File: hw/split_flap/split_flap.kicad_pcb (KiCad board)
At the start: 2 copper layers, 104.5 x 98.3 mm, 42 parts, among them J1 Conn_01x02, J10 Conn_01x05, J11 Conn_01x05, J12 Conn_01x05, J13 Conn_01x05, J14 Conn_01x05, J15 Conn_01x05, J16 Conn_01x05, J19 POWER, J2 Conn_01x02, J3 Conn_01x02, J4 Conn_01x02, J5 Conn_01x02, J6 Conn_01x02, J7 Conn_01x02, J8 Conn_01x02, J9 Conn_01x05, SW1 SW_RESET, U1 PCF8574, U10 ULN2803A, U2 NodeMCU_1.0_(ESP-12E), U3 PCF8574, U4 ULN2803A, U5 PCF8574, U6 ULN2803A, U7 PCF8574, U8 ULN2803A, U9 PCF8574

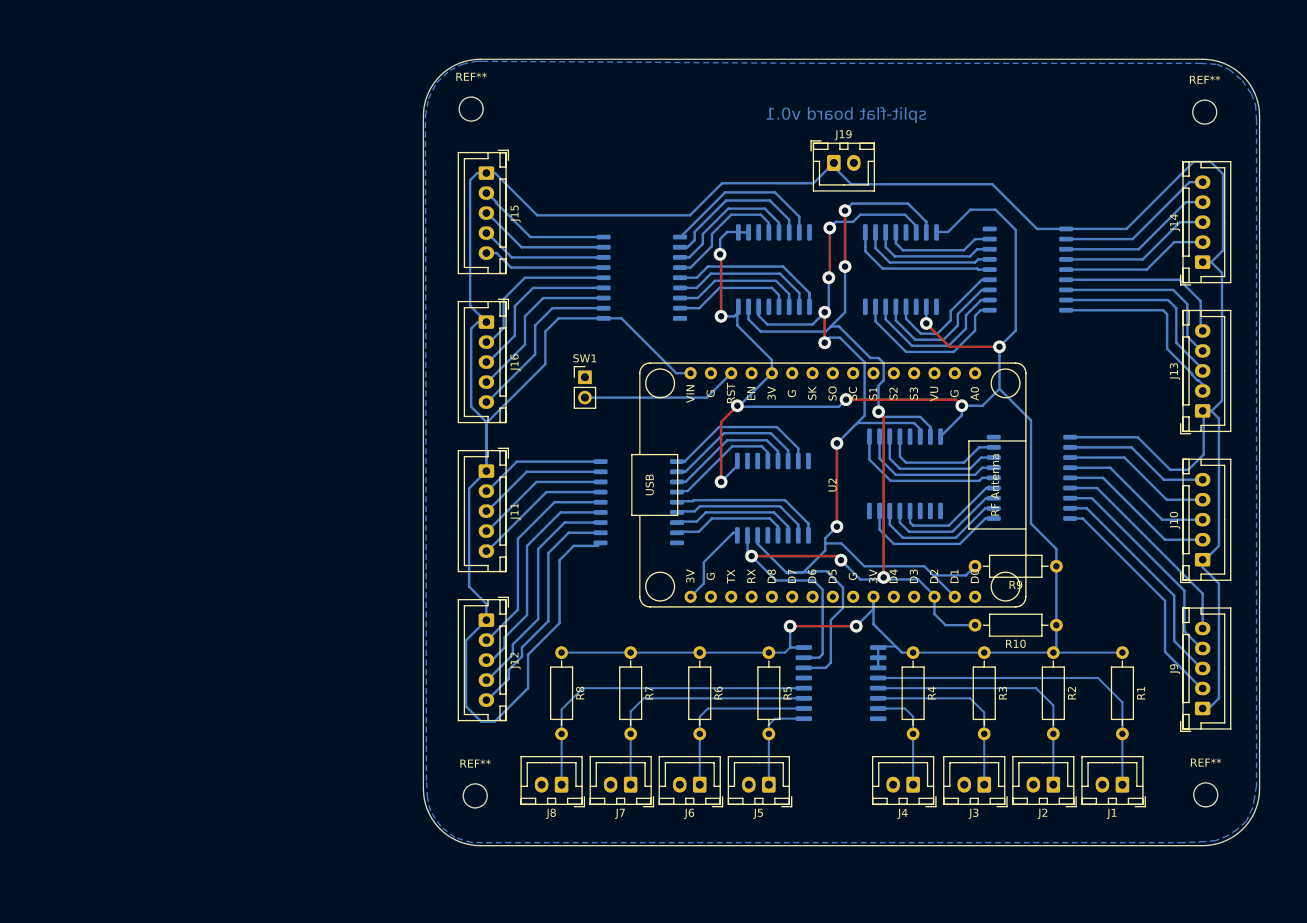
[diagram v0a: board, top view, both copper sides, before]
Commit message: Add missing Interrupt line
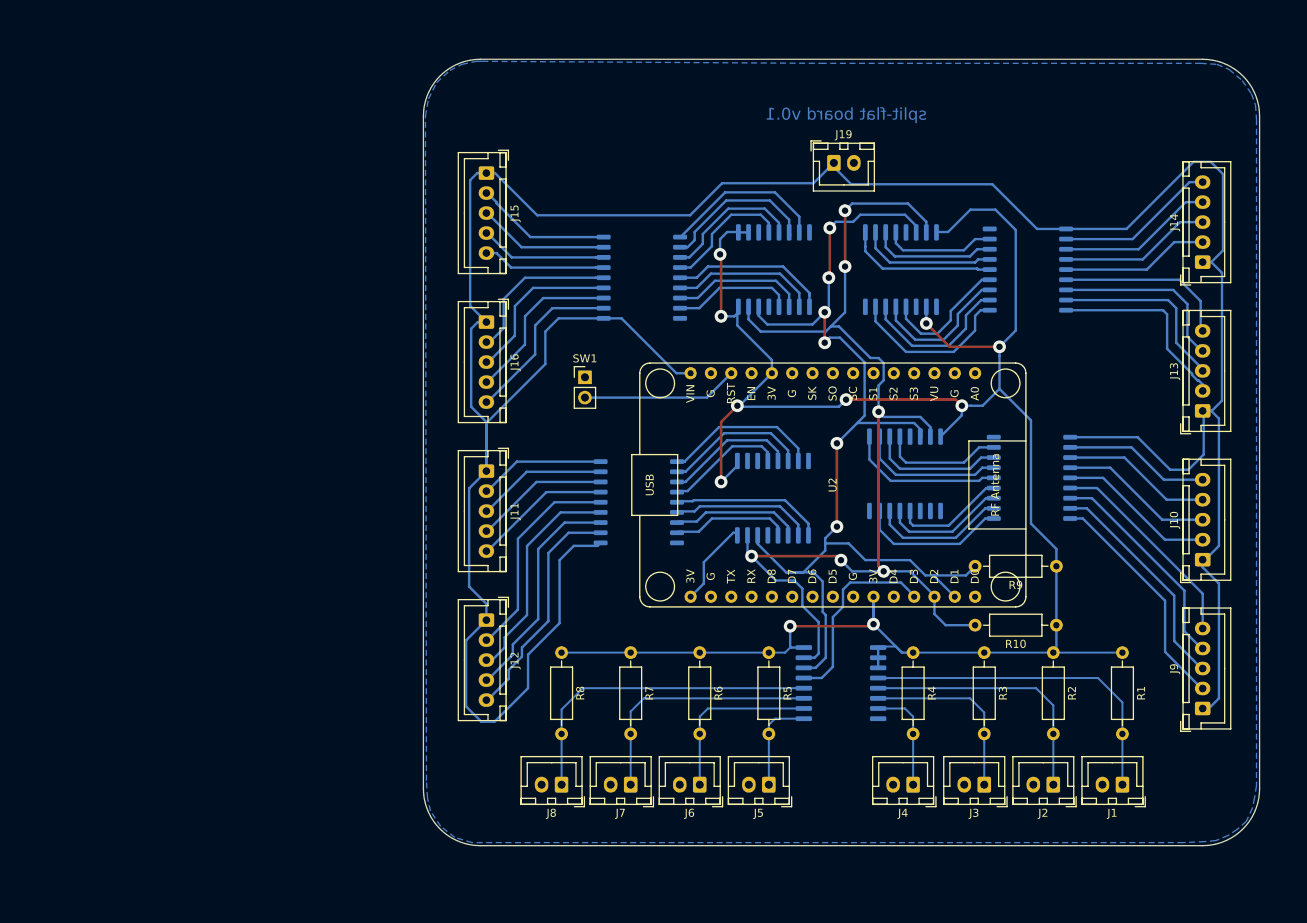
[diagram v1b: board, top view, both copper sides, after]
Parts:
- removed REF** (x4): MountingHole_3mm, MountingHole:MountingHole_3mm
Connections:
- U1 pad 13: (no net) -> /INT
- U2 pad 27: (no net) -> /INT
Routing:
- net /INT: track 0.00 -> 24.5 mm
- net /SCL: track 137.1 -> 133.4 mm
- net /SDA: track 142.3 -> 138.9 mm
- net +3V3: track 264.5 -> 265.6 mm

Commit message: hw: Supercharge PCB !
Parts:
- removed SW1: SW_RESET, Connector_PinHeader_2.54mm:PinHeader_1x02_P2.54mm_Vertical
- added J17: Conn_01x05, Connector_JST:JST_XH_B5B-XH-A_1x05_P2.50mm_Vertical, F.Cu at (144.4, 99.7)
- added J18: Conn_01x05, Connector_JST:JST_XH_B5B-XH-A_1x05_P2.50mm_Vertical, F.Cu at (194.9, 63.8)
- added J20: Conn_01x05, Connector_JST:JST_XH_B5B-XH-A_1x05_P2.50mm_Vertical, F.Cu at (179.5, 45.8)
- added J21: Conn_01x05, Connector_JST:JST_XH_B5B-XH-A_1x05_P2.50mm_Vertical, F.Cu at (108.3, 45.6)
- added J22: Conn_01x05, Connector_JST:JST_XH_B5B-XH-A_1x05_P2.50mm_Vertical, F.Cu at (102.1, 53.6)
- added J23: Conn_01x02, Connector_JST:JST_XH_B2B-XH-A_1x02_P2.50mm_Vertical, F.Cu at (130.6, 91.6)
- added J24: Conn_01x02, Connector_JST:JST_XH_B2B-XH-A_1x02_P2.50mm_Vertical, F.Cu at (130.6, 83.1)
- added J25: Conn_01x02, Connector_JST:JST_XH_B2B-XH-A_1x02_P2.50mm_Vertical, F.Cu at (166.5, 80.4)
- added J26: Conn_01x02, Connector_JST:JST_XH_B2B-XH-A_1x02_P2.50mm_Vertical, F.Cu at (166.5, 88.9)
- added R11: R, Resistor_THT:R_Axial_DIN0207_L6.3mm_D2.5mm_P10.16mm_Horizontal, F.Cu at (126.0, 97.3)
- added R12: R, Resistor_THT:R_Axial_DIN0207_L6.3mm_D2.5mm_P10.16mm_Horizontal, F.Cu at (126.0, 74.8)
- added R13: R, Resistor_THT:R_Axial_DIN0207_L6.3mm_D2.5mm_P10.16mm_Horizontal, F.Cu at (171.2, 74.5)
- added R14: R, Resistor_THT:R_Axial_DIN0207_L6.3mm_D2.5mm_P10.16mm_Horizontal, F.Cu at (171.2, 97.3)
- added U11: PCF8574, Package_SO:SOIC-16W_7.5x10.3mm_P1.27mm, B.Cu at (171.7, 58.9)
- added U12: ULN2803A, Package_SO:SOP-18_7x12.5mm_P1.27mm, B.Cu at (184.8, 58.7)
- added U13: PCF8574, Package_SO:SOIC-16W_7.5x10.3mm_P1.27mm, B.Cu at (125.6, 59.1)
- added U14: ULN2803A, Package_SO:SOP-18_7x12.5mm_P1.27mm, B.Cu at (111.9, 58.9)
- added U15: PCF8574, Package_SO:SOIC-16W_7.5x10.3mm_P1.27mm, B.Cu at (149.4, 83.2)
- U2: footprint ESP:NodeMCU1.0(12-E) -> ESP:ESP12F-Devkit-V3
- moved J15 99.4 mm to (194.9, 96.1), turned to 90 degrees
- moved J14 91.8 mm to (102.1, 69.8), turned to 270 degrees
- moved J13 91.7 mm to (102.1, 86.0), turned to 270 degrees
- moved J16 90.9 mm to (194.9, 80.0), turned to 90 degrees
- moved U10 60.4 mm to (180.5, 89.0), turned to 270 degrees
- moved R10 59.9 mm to (147.8, 58.8), turned to 270 degrees
- moved U8 59.3 mm to (116.6, 88.8), turned to 270 degrees
- moved J19 54.4 mm to (148.2, 108.5)
- moved R9 49.7 mm to (150.9, 61.3), turned to 270 degrees
- moved U9 41.0 mm to (180.5, 75.3), turned to 180 degrees
- moved U7 40.1 mm to (116.7, 75.2), turned to 180 degrees
- moved U2 27.2 mm to (148.7, 67.2), turned to 180 degrees
- moved U3 17.4 mm to (166.8, 107.1), turned to 270 degrees
- moved U4 15.8 mm to (180.6, 107.1)
- moved U5 13.9 mm to (130.7, 106.3), turned to 90 degrees
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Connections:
- U10 pad 1: Net-(U10-Pad1) -> /sheet5DE57FF1/L5
- U10 pad 11: Net-(J16-Pad5) -> Net-(J16-Pad2)
- U10 pad 12: Net-(J16-Pad4) -> Net-(J16-Pad3)
- U10 pad 13: Net-(J16-Pad3) -> Net-(J16-Pad4)
- U10 pad 14: Net-(J16-Pad2) -> Net-(J16-Pad5)
- U10 pad 2: Net-(U10-Pad2) -> /sheet5DE57FF1/L6
- U10 pad 3: Net-(U10-Pad3) -> /sheet5DE57FF1/L7
- U10 pad 4: Net-(U10-Pad4) -> /sheet5DE57FF1/L8
- U10 pad 5: Net-(U10-Pad5) -> /sheet5DE57FF1/L1
- U10 pad 6: Net-(U10-Pad6) -> /sheet5DE57FF1/L2
- U10 pad 7: Net-(U10-Pad7) -> /sheet5DE57FF1/L3
- U10 pad 8: Net-(U10-Pad8) -> /sheet5DE57FF1/L4
- U2 pad 13: Net-(SW1-Pad2) -> (no net)
- U2 pad 14: GND -> (no net)
- U2 pad 27: /INT -> (no net)
- U2 pad 30: (no net) -> /INT
- U3 pad 10: Net-(U3-Pad10) -> /SheetMotor1/L6
- U3 pad 11: Net-(U3-Pad11) -> /SheetMotor1/L7
- U3 pad 12: Net-(U3-Pad12) -> /SheetMotor1/L8
- U3 pad 4: Net-(U3-Pad4) -> /SheetMotor1/L1
- U3 pad 5: Net-(U3-Pad5) -> /SheetMotor1/L2
- U3 pad 6: Net-(U3-Pad6) -> /SheetMotor1/L3
- U3 pad 7: Net-(U3-Pad7) -> /SheetMotor1/L4
- U3 pad 9: Net-(U3-Pad9) -> /SheetMotor1/L5
- U4 pad 1: Net-(U3-Pad7) -> /SheetMotor1/L5
- U4 pad 2: Net-(U3-Pad6) -> /SheetMotor1/L6
- U4 pad 3: Net-(U3-Pad5) -> /SheetMotor1/L7
- U4 pad 4: Net-(U3-Pad4) -> /SheetMotor1/L8
- U4 pad 5: Net-(U3-Pad9) -> /SheetMotor1/L1
- U4 pad 6: Net-(U3-Pad10) -> /SheetMotor1/L2
- U4 pad 7: Net-(U3-Pad11) -> /SheetMotor1/L3
- U4 pad 8: Net-(U3-Pad12) -> /SheetMotor1/L4
- U5 pad 10: Net-(U5-Pad10) -> /sheetMotor2/L6
- U5 pad 11: Net-(U5-Pad11) -> /sheetMotor2/L7
- U5 pad 12: Net-(U5-Pad12) -> /sheetMotor2/L8
- U5 pad 4: Net-(U5-Pad4) -> /sheetMotor2/L1
- U5 pad 5: Net-(U5-Pad5) -> /sheetMotor2/L2
- U5 pad 6: Net-(U5-Pad6) -> /sheetMotor2/L3
- U5 pad 7: Net-(U5-Pad7) -> /sheetMotor2/L4
- U5 pad 9: Net-(U5-Pad9) -> /sheetMotor2/L5
- U6 pad 1: Net-(U5-Pad7) -> /sheetMotor2/L5
- U6 pad 2: Net-(U5-Pad6) -> /sheetMotor2/L6
- U6 pad 3: Net-(U5-Pad5) -> /sheetMotor2/L7
- U6 pad 4: Net-(U5-Pad4) -> /sheetMotor2/L8
- U6 pad 5: Net-(U5-Pad9) -> /sheetMotor2/L1
- U6 pad 6: Net-(U5-Pad10) -> /sheetMotor2/L2
- U6 pad 7: Net-(U5-Pad11) -> /sheetMotor2/L3
- U6 pad 8: Net-(U5-Pad12) -> /sheetMotor2/L4
- U7 pad 10: Net-(U7-Pad10) -> /Sheet5DE1D348/L6
- U7 pad 11: Net-(U7-Pad11) -> /Sheet5DE1D348/L7
- U7 pad 12: Net-(U7-Pad12) -> /Sheet5DE1D348/L8
- U7 pad 4: Net-(U7-Pad4) -> /Sheet5DE1D348/L1
- U7 pad 5: Net-(U7-Pad5) -> /Sheet5DE1D348/L2
- U7 pad 6: Net-(U7-Pad6) -> /Sheet5DE1D348/L3
- U7 pad 7: Net-(U7-Pad7) -> /Sheet5DE1D348/L4
- U7 pad 9: Net-(U7-Pad9) -> /Sheet5DE1D348/L5
- U8 pad 1: Net-(U7-Pad7) -> /Sheet5DE1D348/L5
- U8 pad 11: Net-(J14-Pad5) -> Net-(J14-Pad2)
- U8 pad 12: Net-(J14-Pad4) -> Net-(J14-Pad3)
- U8 pad 13: Net-(J14-Pad3) -> Net-(J14-Pad4)
- U8 pad 14: Net-(J14-Pad2) -> Net-(J14-Pad5)
- U8 pad 2: Net-(U7-Pad6) -> /Sheet5DE1D348/L6
- U8 pad 3: Net-(U7-Pad5) -> /Sheet5DE1D348/L7
- U8 pad 4: Net-(U7-Pad4) -> /Sheet5DE1D348/L8
- U8 pad 5: Net-(U7-Pad9) -> /Sheet5DE1D348/L1
- U8 pad 6: Net-(U7-Pad10) -> /Sheet5DE1D348/L2
- U8 pad 7: Net-(U7-Pad11) -> /Sheet5DE1D348/L3
- U8 pad 8: Net-(U7-Pad12) -> /Sheet5DE1D348/L4
- U9 pad 10: Net-(U10-Pad6) -> /sheet5DE57FF1/L6
- U9 pad 11: Net-(U10-Pad7) -> /sheet5DE57FF1/L7
- U9 pad 12: Net-(U10-Pad8) -> /sheet5DE57FF1/L8
- U9 pad 4: Net-(U10-Pad4) -> /sheet5DE57FF1/L1
- U9 pad 5: Net-(U10-Pad3) -> /sheet5DE57FF1/L2
- U9 pad 6: Net-(U10-Pad2) -> /sheet5DE57FF1/L3
- U9 pad 7: Net-(U10-Pad1) -> /sheet5DE57FF1/L4
- U9 pad 9: Net-(U10-Pad5) -> /sheet5DE57FF1/L5
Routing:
- net +5V: track 355.0 -> 0.00 mm
- net +3V3: track 265.6 -> 64.5 mm, vias 10 -> 0
- net /SDA: track 138.9 -> 0.00 mm, vias 6 -> 0
- net /SCL: track 133.4 -> 0.00 mm, vias 6 -> 0
- net Net-(J12-Pad5): track 29.2 -> 0.00 mm
- net Net-(J9-Pad2): track 29.1 -> 0.00 mm
- net Net-(J12-Pad4): track 28.3 -> 0.00 mm
- net Net-(J9-Pad3): track 28.2 -> 0.00 mm
- net Net-(J12-Pad3): track 27.7 -> 0.00 mm
- net Net-(J9-Pad4): track 27.3 -> 0.00 mm
- net Net-(J12-Pad2): track 26.6 -> 0.00 mm
- net Net-(J9-Pad5): track 26.4 -> 0.00 mm
- net /INT: track 24.5 -> 0.00 mm
- net Net-(J13-Pad2): track 24.3 -> 0.00 mm
- net Net-(J13-Pad3): track 23.4 -> 0.00 mm
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- removed copper zone on B.Cu, net GND
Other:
- board text removed: "split-flat board v0.1"

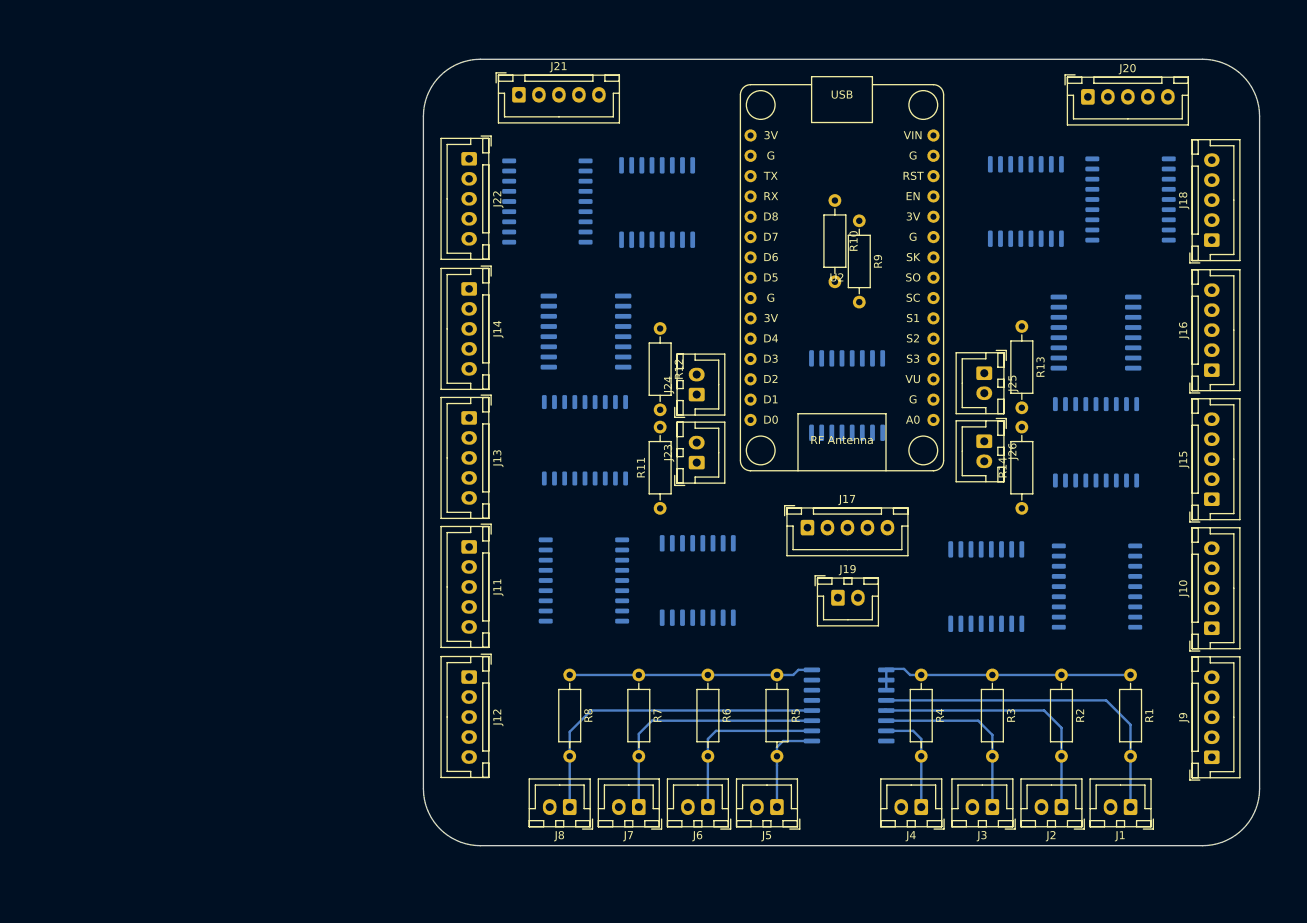
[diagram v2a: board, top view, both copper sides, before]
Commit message: Reroute full PCB
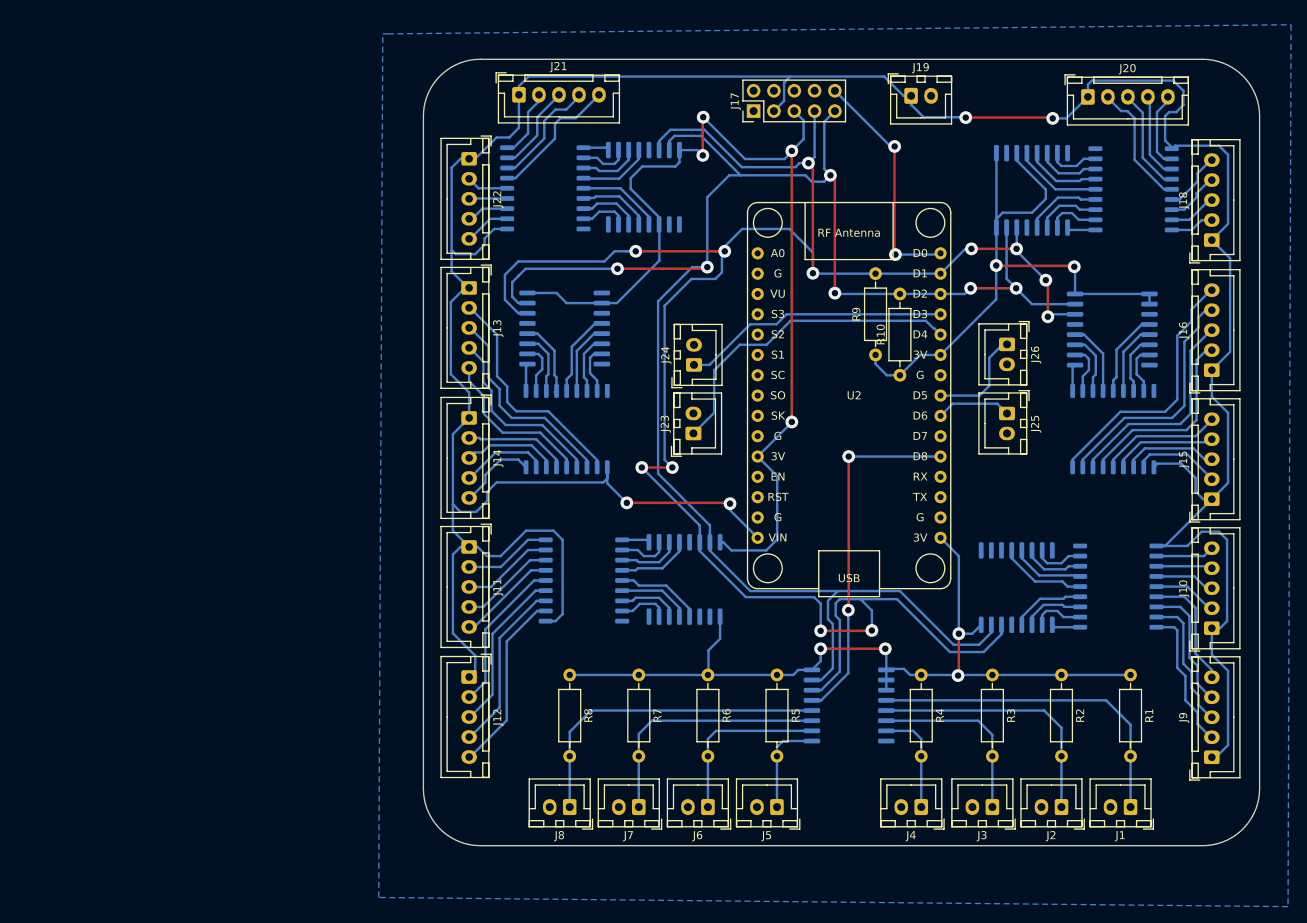
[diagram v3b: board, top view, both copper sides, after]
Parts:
- removed R11, R12, R13, R14: R, Resistor_THT:R_Axial_DIN0207_L6.3mm_D2.5mm_P10.16mm_Horizontal
- removed U15: PCF8574, Package_SO:SOIC-16W_7.5x10.3mm_P1.27mm
- J17: value Conn_01x05 -> EXPANDER_PORT; footprint Connector_JST:JST_XH_B5B-XH-A_1x05_P2.50mm_Vertical -> Connector_PinHeader_2.54mm:PinHeader_2x05_P2.54mm_Vertical
- moved J19 63.4 mm to (157.4, 45.7)
- moved J17 52.5 mm to (137.7, 47.6), turned to 90 degrees
- moved R10 23.3 mm to (156.0, 80.6), turned to 90 degrees
- moved U2 17.3 mm to (149.6, 84.5), turned to 0 degrees
- moved R9 16.9 mm to (152.9, 78.1), turned to 90 degrees
- moved J13 16.3 mm to (102.1, 69.7)
- moved J14 16.1 mm to (102.1, 86.0)
- moved J26 12.4 mm to (169.3, 76.8)
- moved J25 5.78 mm to (169.3, 85.4)
- moved U3 3.81 mm to (170.6, 107.2)
- moved J24 3.72 mm to (130.2, 79.3)
- moved J23 3.67 mm to (130.1, 87.9)
- moved U10 2.72 mm to (182.6, 87.4)
- moved U7 2.69 mm to (114.0, 74.8)
- moved U8 2.68 mm to (114.3, 87.4)
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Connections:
- J17 pad 1: +5V -> GND
- J17 pad 2: +3V3 -> GND
- J17 pad 3: GND -> +5V
- J17 pad 4: /SCL -> (no net)
- J17 pad 5: /SDA -> +3V3
- J23 pad 1: Net-(J23-Pad1) -> /EXT_INT4
- J24 pad 1: Net-(J24-Pad1) -> /EXT_INT3
- J25 pad 1: Net-(J25-Pad1) -> /EXT_INT2
- J26 pad 1: Net-(J26-Pad1) -> /EXT_INT1
- U10 pad 11: Net-(J16-Pad2) -> Net-(J15-Pad2)
- U10 pad 12: Net-(J16-Pad3) -> Net-(J15-Pad3)
- U10 pad 13: Net-(J16-Pad4) -> Net-(J15-Pad4)
- U10 pad 14: Net-(J16-Pad5) -> Net-(J15-Pad5)
- U10 pad 15: Net-(J15-Pad5) -> Net-(J16-Pad2)
- U10 pad 16: Net-(J15-Pad4) -> Net-(J16-Pad3)
- U10 pad 17: Net-(J15-Pad3) -> Net-(J16-Pad4)
- U10 pad 18: Net-(J15-Pad2) -> Net-(J16-Pad5)
- U2 pad 14: (no net) -> GND
- U2 pad 20: (no net) -> /INT
- U2 pad 22: (no net) -> /EXT_INT2
- U2 pad 23: (no net) -> /EXT_INT1
- U2 pad 26: (no net) -> /EXT_INT4
- U2 pad 27: (no net) -> /EXT_INT3
- U2 pad 30: /INT -> /EXP_INT
- U8 pad 11: Net-(J14-Pad2) -> Net-(J13-Pad2)
- U8 pad 12: Net-(J14-Pad3) -> Net-(J13-Pad3)
- U8 pad 13: Net-(J14-Pad4) -> Net-(J13-Pad4)
- U8 pad 14: Net-(J14-Pad5) -> Net-(J13-Pad5)
- U8 pad 15: Net-(J13-Pad5) -> Net-(J14-Pad2)
- U8 pad 16: Net-(J13-Pad4) -> Net-(J14-Pad3)
- U8 pad 17: Net-(J13-Pad3) -> Net-(J14-Pad4)
- U8 pad 18: Net-(J13-Pad2) -> Net-(J14-Pad5)
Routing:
- net +5V: track 0.00 -> 388.3 mm, vias 0 -> 4
- net /SCL: track 0.00 -> 258.7 mm, vias 0 -> 12
- net +3V3: track 64.5 -> 313.0 mm, vias 0 -> 10
- net /SDA: track 0.00 -> 227.7 mm, vias 0 -> 6
- net /INT: track 0.00 -> 44.5 mm, vias 0 -> 2
- net /EXT_INT4: track 0.00 -> 40.5 mm
- net /EXT_INT3: track 0.00 -> 33.4 mm
- net Net-(J16-Pad5): track 0.00 -> 32.7 mm
- net Net-(J16-Pad4): track 0.00 -> 30.3 mm
- net /EXP_INT: track 0.00 -> 29.6 mm, vias 0 -> 2
- net Net-(J13-Pad2): track 0.00 -> 29.0 mm
- net Net-(J16-Pad3): track 0.00 -> 27.1 mm
- net Net-(J13-Pad3): track 0.00 -> 26.0 mm
- net Net-(J16-Pad2): track 0.00 -> 24.6 mm
- net Net-(J13-Pad4): track 0.00 -> 23.2 mm
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- added copper zone on B.Cu, net GND
